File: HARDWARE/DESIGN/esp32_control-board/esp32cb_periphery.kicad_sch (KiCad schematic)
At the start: 29 parts, among them J1 Conn_02x03_Counter_Clockwise, U304 TPD2E2U06DRL, U307 TPD4E05U06DQA, U5 PC817, U6 TBD62783A, U7 MCP23008-xSS, U8 MCP23008-xSS, U9 TBD62783A

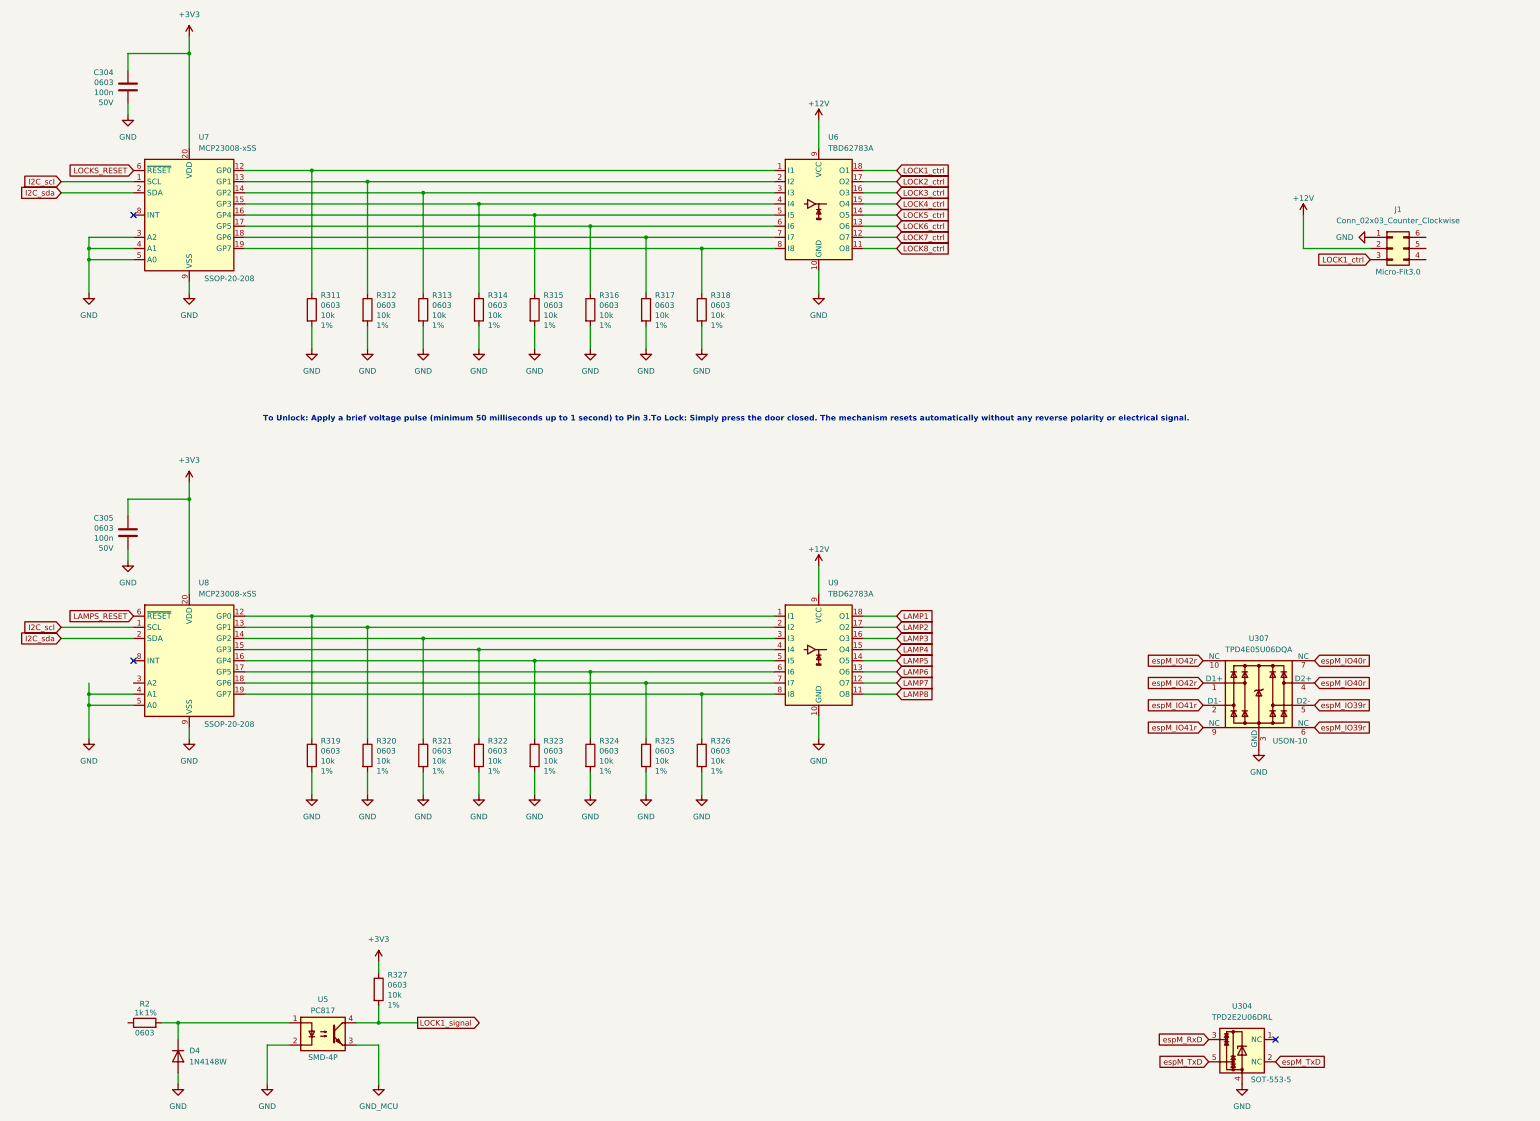
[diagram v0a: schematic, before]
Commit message: 60707 - schematics and readme updated, preliminary PCB-layout prepared
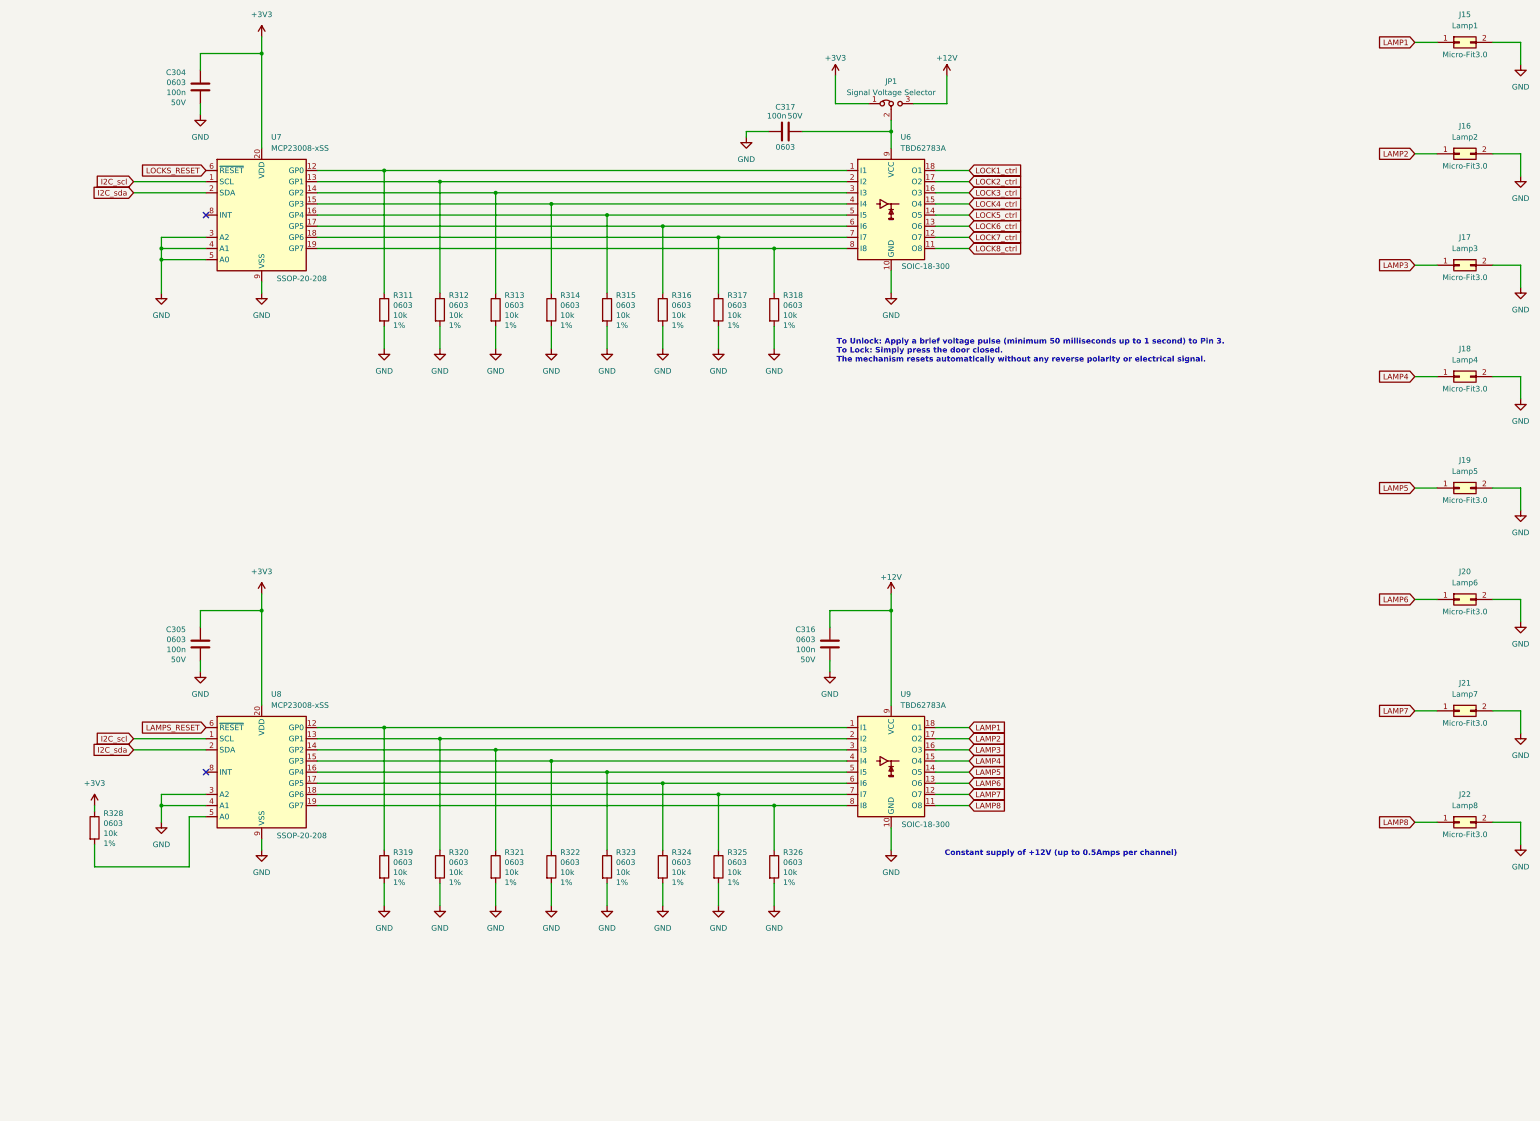
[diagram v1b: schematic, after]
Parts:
- removed D4: 1N4148W, Diode_SMD:D_SOD-123, symbol Diode:1N4148W
- removed J1: Conn_02x03_Counter_Clockwise, Connector_Molex:Molex_Micro-Fit_3.0_43045-0600_2x03_P3.00mm_Horizontal, symbol Connector_Generic:Conn_02x03_Counter_Clockwise
- removed R2: 1k, Resistor_SMD:R_0603_1608Metric, symbol Device:R
- removed R327: 10k, Resistor_SMD:R_0603_1608Metric, symbol Device:R
- removed U304: TPD2E2U06DRL, Package_TO_SOT_SMD:SOT-553, symbol Power_Protection:TPD2E2U06DRL
- removed U307: TPD4E05U06DQA, Package_SON:USON-10_2.5x1.0mm_P0.5mm, symbol Power_Protection:TPD4E05U06DQA
- removed U5: PC817, Package_DIP:DIP-4_W7.62mm, symbol Isolator:PC817
- added C316, C317: 100n, Capacitor_SMD:C_0603_1608Metric, symbol Device:C
- added J15: Lamp1, Connector_Molex:Molex_Micro-Fit_3.0_43045-0200_2x01_P3.00mm_Horizontal, symbol Connector_Generic:Conn_02x01
- added J16: Lamp2, Connector_Molex:Molex_Micro-Fit_3.0_43045-0200_2x01_P3.00mm_Horizontal, symbol Connector_Generic:Conn_02x01
- added J17: Lamp3, Connector_Molex:Molex_Micro-Fit_3.0_43045-0200_2x01_P3.00mm_Horizontal, symbol Connector_Generic:Conn_02x01
- added J18: Lamp4, Connector_Molex:Molex_Micro-Fit_3.0_43045-0200_2x01_P3.00mm_Horizontal, symbol Connector_Generic:Conn_02x01
- added J19: Lamp5, Connector_Molex:Molex_Micro-Fit_3.0_43045-0200_2x01_P3.00mm_Horizontal, symbol Connector_Generic:Conn_02x01
- added J20: Lamp6, Connector_Molex:Molex_Micro-Fit_3.0_43045-0200_2x01_P3.00mm_Horizontal, symbol Connector_Generic:Conn_02x01
- added J21: Lamp7, Connector_Molex:Molex_Micro-Fit_3.0_43045-0200_2x01_P3.00mm_Horizontal, symbol Connector_Generic:Conn_02x01
- added J22: Lamp8, Connector_Molex:Molex_Micro-Fit_3.0_43045-0200_2x01_P3.00mm_Horizontal, symbol Connector_Generic:Conn_02x01
- added JP1: Signal Voltage Selector, Jumper:SolderJumper-3_P1.3mm_Bridged12_RoundedPad1.0x1.5mm, symbol Jumper:Jumper_3_Bridged12
- added R328: 10k, Resistor_SMD:R_0603_1608Metric, symbol Device:R
- U6, U9: footprint (none) -> Package_SO:SOIC-18W_7.5x11.6mm_P1.27mm; LCSC (none) -> C146353; Manufacturer (none) -> TOSHIBA; Package (none) -> SOIC-18-300
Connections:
- net +12V: now also C316.2, JP1.3 (B); no longer U6.9 (VCC)
- net +3V3: now also JP1.1 (A), R328.1
- net GND: now also U8.3 (A2), C316.1, C317.1, J15.2 (Pin_2), J16.2 (Pin_2), J17.2 (Pin_2), J18.2 (Pin_2), J19.2 (Pin_2), J20.2 (Pin_2), J21.2 (Pin_2), J22.2 (Pin_2); no longer U8.5 (A0)
- net LAMP1: now also J15.1 (Pin_1)
- net LAMP2: now also J16.1 (Pin_1)
- net LAMP3: now also J17.1 (Pin_1)
- net LAMP4: now also J18.1 (Pin_1)
- net LAMP5: now also J19.1 (Pin_1)
- net LAMP6: now also J20.1 (Pin_1)
- net LAMP7: now also J21.1 (Pin_1)
- net LAMP8: now also J22.1 (Pin_1)
- new net: C317.2, JP1.2 (C), U6.9 (VCC)
- new net: R328.2, U8.5 (A0)
- no-connect marks 3 -> 2
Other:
- note added: "Constant supply of +12V (up to 0.5Amps per channel)"
- note added: "To Unlock: Apply a brief voltage pulse (minimum 50 milliseconds up to 1 second) to Pin 3. To Lock: Simply press the door closed. The mechanism resets automatically without any reverse polarity or electrical signal."
- note removed: "To Unlock: Apply a brief voltage pulse (minimum 50 milliseconds up to 1 second) to Pin 3.To Lock: Simply press the door closed. The mechanism resets automatically without any reverse polarity or electrical signal."
- title: (none) -> ESP32-based Control Board
- moved on the sheet: C304, C305, R311, R312, R313, R314, R315, R316, R317, R318, R319, R320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

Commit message: 60710 - schematic and PCB-layout updated
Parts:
- added D13, D24, D25, D26, D27, D28, D29, D30: LOCK on, LED_SMD:LED_0603_1608Metric, symbol Device:LED
- added D16, D17, D18, D19, D20, D21, D22, D23: LAMP on, LED_SMD:LED_0603_1608Metric, symbol Device:LED
- added R307: 12k, Resistor_SMD:R_0603_1608Metric, symbol Device:R
- added R344, R345, R346, R347, R348, R349, R350, R351, R352, R353, R354, R355, R356, R357, R358: 5k1, Resistor_SMD:R_0603_1608Metric, symbol Device:R
- R311, R312, R313, R314, R315, R316, R317, R318, R319, R320, R321, R322, R323, R324, R325, R326: value 10k -> 12k; LCSC (none) -> C2907097; LCSC part C25804 -> (none); Manufacturer UNI-ROYAL -> FOJAN; Property 1% -> 5%
- R328: value 10k -> 5k1; LCSC part C25804 -> C2907044; Manufacturer UNI-ROYAL -> FOJAN; now in the parts list
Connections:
- net +3V3: now also R326.1; no longer R328.1
- net GND: now also C317.2, D13.1 (K), D16.1 (K), D17.1 (K), D18.1 (K), D19.1 (K), D20.1 (K), D21.1 (K), D22.1 (K), D23.1 (K), D24.1 (K), D25.1 (K), D26.1 (K), D27.1 (K), D28.1 (K), D29.1 (K), D30.1 (K), R307.2; no longer C317.1, R326.2
- net LAMP1: now also U9.11 (O8), R344.2; no longer U9.18 (O1)
- net LAMP2: now also U9.12 (O7), R345.2; no longer U9.17 (O2)
- net LAMP3: now also U9.13 (O6), R347.2; no longer U9.16 (O3)
- net LAMP4: now also U9.14 (O5), R346.2; no longer U9.15 (O4)
- net LAMP5: now also U9.15 (O4), R348.2; no longer U9.14 (O5)
- net LAMP6: now also U9.16 (O3), R349.2; no longer U9.13 (O6)
- net LAMP7: now also U9.17 (O2), R351.2; no longer U9.12 (O7)
- net LAMP8: now also U9.18 (O1), R350.2; no longer U9.11 (O8)
- net LOCK1_ctrl: now also R328.2, U6.11 (O8); no longer U6.18 (O1)
- net LOCK2_ctrl: now also U6.12 (O7), R352.2; no longer U6.17 (O2)
- net LOCK3_ctrl: now also U6.13 (O6), R353.2; no longer U6.16 (O3)
- net LOCK4_ctrl: now also U6.14 (O5), R354.2; no longer U6.15 (O4)
- net LOCK5_ctrl: now also U6.15 (O4), R355.2; no longer U6.14 (O5)
- net LOCK6_ctrl: now also U6.16 (O3), R356.2; no longer U6.13 (O6)
- net LOCK7_ctrl: now also U6.17 (O2), R357.2; no longer U6.12 (O7)
- net LOCK8_ctrl: now also U6.18 (O1), R358.2; no longer U6.11 (O8)
- net at R314.1, U6.4 (I4): now also U7.16 (GP4); no longer U7.15 (GP3)
- net at JP1.2 (C), U6.9 (VCC): now also C317.1; no longer C317.2
- net at R322.1, U9.4 (I4): now also U8.16 (GP4); no longer U8.15 (GP3)
- net at U8.5 (A0): now also R326.2; no longer R328.2
- new net: D25.2 (A), R353.1
- new net: D16.2 (A), R344.1
- new net: D24.2 (A), R352.1
- new net: R317.1, U6.1 (I1), U7.19 (GP7)
- new net: R316.1, U6.2 (I2), U7.18 (GP6)
- new net: R315.1, U6.3 (I3), U7.17 (GP5)
- new net: R313.1, U6.5 (I5), U7.15 (GP3)
- new net: R312.1, U6.6 (I6), U7.14 (GP2)
- new net: R311.1, U6.7 (I7), U7.13 (GP1)
- new net: R307.1, U6.8 (I8), U7.12 (GP0)
- new net: D19.2 (A), R347.1
- new net: R321.1, U8.15 (GP3), U9.5 (I5)
- new net: D28.2 (A), R356.1
- new net: R318.1, U8.12 (GP0), U9.8 (I8)
- new net: D26.2 (A), R354.1
- new net: R320.1, U8.14 (GP2), U9.6 (I6)
- new net: D30.2 (A), R358.1
- new net: D21.2 (A), R349.1
- new net: D27.2 (A), R355.1
- new net: R323.1, U8.17 (GP5), U9.3 (I3)
- new net: D20.2 (A), R348.1
- new net: D13.2 (A), R328.1
- new net: R325.1, U8.19 (GP7), U9.1 (I1)
- new net: D17.2 (A), R345.1
- new net: R319.1, U8.13 (GP1), U9.7 (I7)
- new net: R324.1, U8.18 (GP6), U9.2 (I2)
- new net: D18.2 (A), R346.1
- new net: D22.2 (A), R350.1
- new net: D29.2 (A), R357.1
- new net: D23.2 (A), R351.1
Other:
- moved on the sheet: C305, C316, C317, J15, J16, J17, J18, J19, J20, J21, J22, JP1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

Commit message: 60714 - one of two I2C-mux ICs was removed, PCB-layout finished, start tracing
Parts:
- removed C304: 100n, Capacitor_SMD:C_0603_1608Metric, symbol Device:C
- removed R326: 12k, Resistor_SMD:R_0603_1608Metric, symbol Device:R
- removed U6: TBD62783A, Package_SO:SOIC-18W_7.5x11.6mm_P1.27mm, symbol Transistor_Array:TBD62783A
- removed U7: MCP23008-xSS, Package_SO:SSOP-20_5.3x7.2mm_P0.65mm, symbol Interface_Expansion:MCP23008-xSS
- added U303: TBD62783A, Package_SO:SOIC-18W_7.5x11.6mm_P1.27mm, symbol Transistor_Array:TBD62783A
- renumbered C305 to C301, C316 to C302, C317 to C303, D13 to D301, D24 to D302, D16 to D303, D17 to D304, D25 to D305, D26 to D306, D19 to D307, D18 to D308, D27 to D309, D28 to D310, D20 to D311, D21 to D312, D29 to D313, D30 to D314, D23 to D315, D22 to D316, J15 to J301, J16 to J302, J17 to J303, J18 to J304, J19 to J305, J20 to J306, J21 to J307, J22 to J308, JP1 to JP301, R328 to R301, R352 to R302, R344 to R303, R345 to R304, R318 to R305, R307 to R306, R319 to R307, R311 to R308, R320 to R309, R312 to R310, R321 to R311, R313 to R312, R353 to R313, R354 to R314, R347 to R315, R346 to R316, R322 to R317, R314 to R318, R323 to R319, R315 to R320, R324 to R321, R316 to R322, R325 to R323, R317 to R324, R355 to R325, R356 to R326, R348 to R327, R349 to R328, R357 to R329, R358 to R330, R351 to R331, R350 to R332, U8 to U301, U9 to U302
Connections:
- net GND: now also U301.5 (A0), U303.10 (GND)
- net LAMP1: now also U302.14 (O5); no longer U302.11 (O8)
- net LAMP2: now also U302.13 (O6); no longer U302.12 (O7)
- net LAMP3: now also U302.11 (O8); no longer U302.13 (O6)
- net LAMP4: now also U302.12 (O7); no longer U302.14 (O5)
- net LAMP7: now also U302.18 (O1); no longer U302.17 (O2)
- net LAMP8: now also U302.17 (O2); no longer U302.18 (O1)
- net LOCK1_ctrl: now also U303.14 (O5)
- net LOCK2_ctrl: now also U303.13 (O6)
- net LOCK3_ctrl: now also U303.11 (O8)
- net LOCK4_ctrl: now also U303.12 (O7)
- net LOCK5_ctrl: now also U303.15 (O4)
- net LOCK6_ctrl: now also U303.16 (O3)
- net LOCK7_ctrl: now also U303.18 (O1)
- net LOCK8_ctrl: now also U303.17 (O2)
- net LOCK8_do: now reaches R324.1
- net LOCK8_do: now also U303.8 (I8)
- net LOCK7_do: now reaches R322.1
- net LOCK7_do: now also U303.7 (I7)
- net LOCK6_do: now reaches R320.1
- net LOCK6_do: now also U303.6 (I6)
- net LOCK5_do: now reaches R318.1
- net LOCK5_do: now also U303.5 (I5)
- net LOCK4_do: now reaches R312.1
- net LOCK4_do: now also U303.4 (I4)
- net LOCK3_do: now reaches R310.1
- net LOCK3_do: now also U303.3 (I3)
- net LOCK2_do: now reaches R308.1
- net LOCK2_do: now also U303.2 (I2)
- net LOCK1_do: now reaches R306.1
- net LOCK1_do: now also U303.1 (I1)
- net at C303.1, JP301.2 (C): now also U303.9 (VCC)
- no-connect marks 2 -> 1
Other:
- moved on the sheet: C303, JP301
